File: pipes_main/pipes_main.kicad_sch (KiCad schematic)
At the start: 51 parts, among them J1 3.5mm Jack, J10 3.5mm Jack, J11 3.5mm Jack, J12 3.5mm Jack, J21 2x8 Female Header, J22 2x5 Female Header, J4 3.5mm Jack, J5 3.5mm Jack, J6 3.5mm Jack, J7 3.5mm Jack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

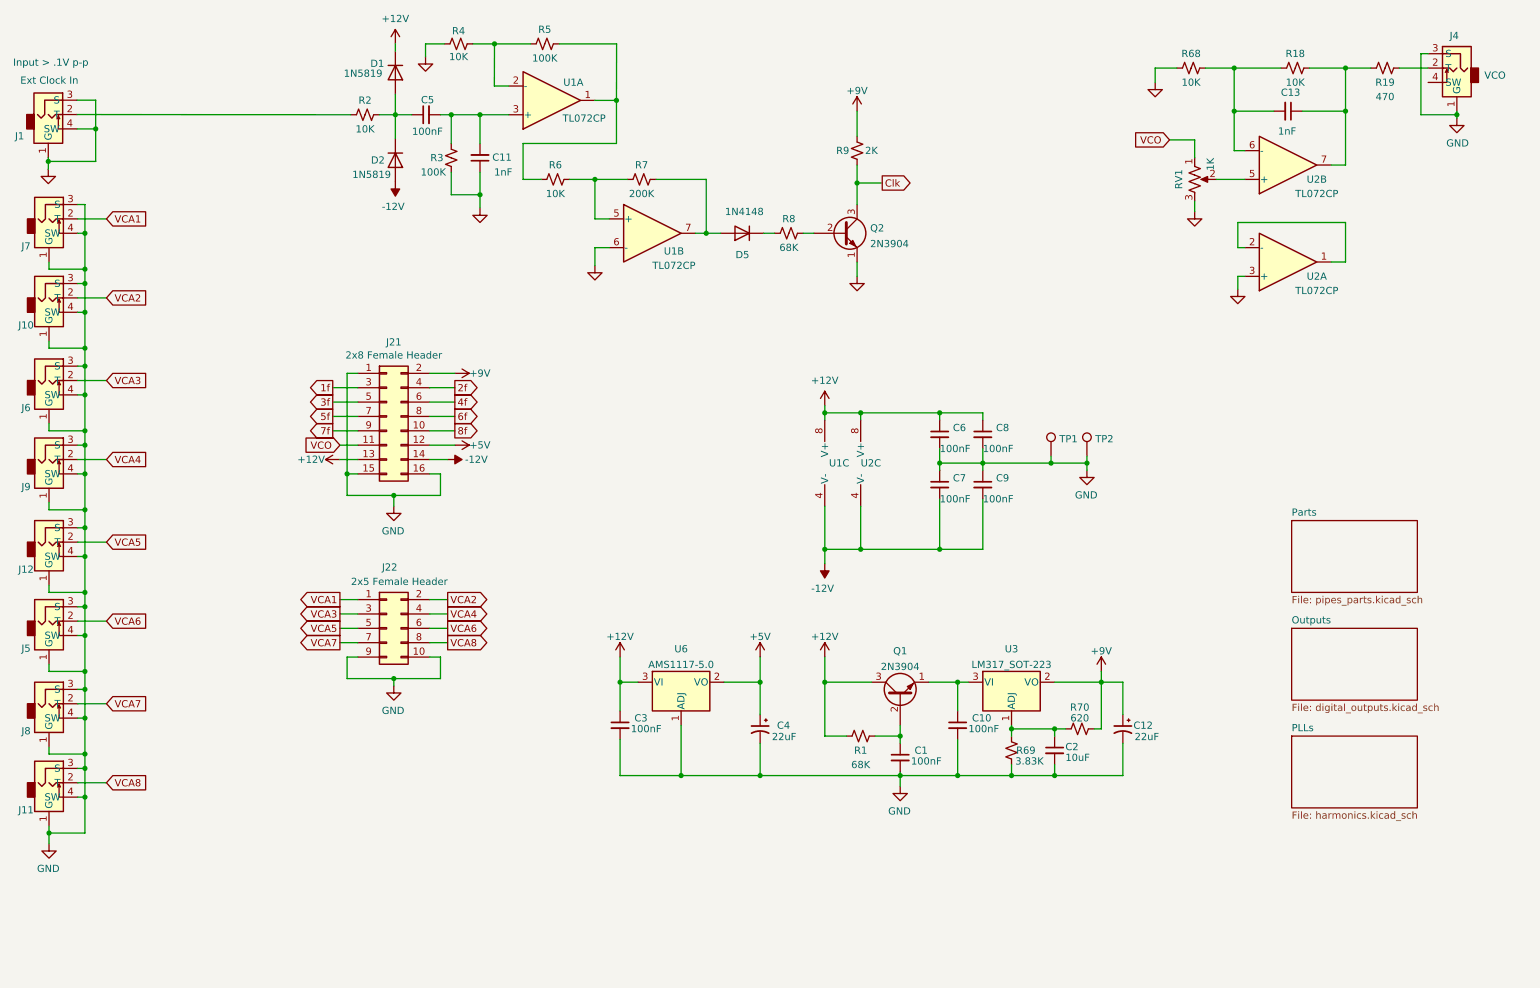
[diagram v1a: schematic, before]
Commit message: Updates component values. Uses .5W resistors on outputs now.
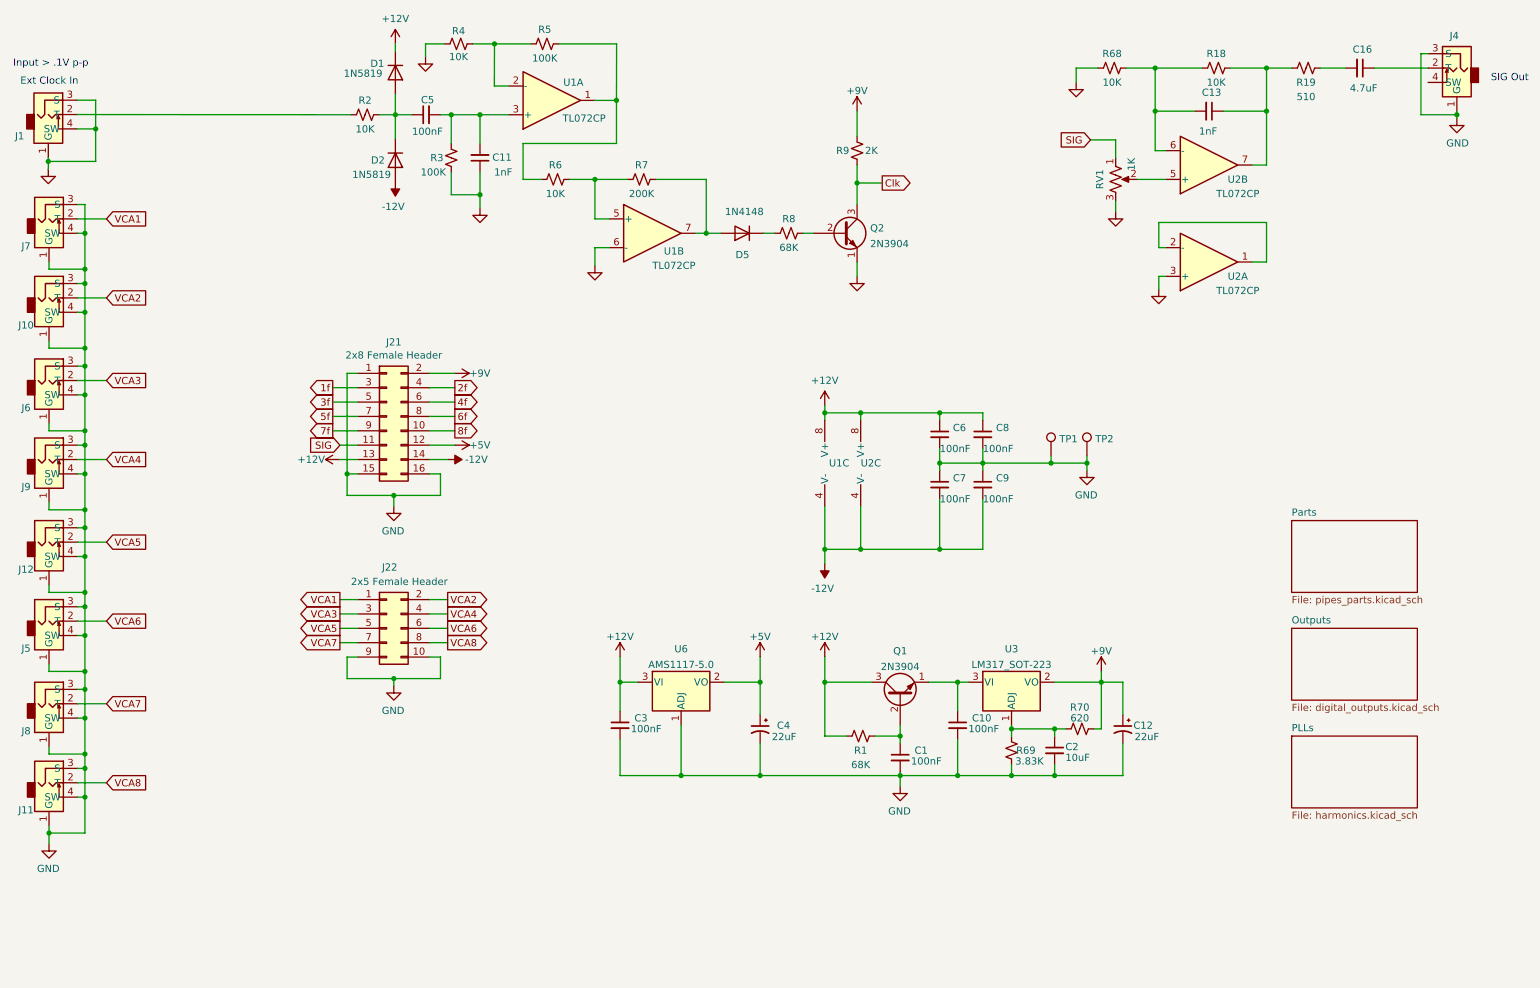
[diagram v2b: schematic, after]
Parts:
- added C16: 4.7uF, Capacitor_SMD:C_1206_3216Metric, symbol Device:C_Small
- R19: value 470 -> 510; LCSC Part # C17710 -> C2842425
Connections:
- net at R19.2: now also C16.2; no longer J4.2 (T)
- net VCO renamed SIG
- new net: C16.1, J4.2 (T)
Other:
- note added: "SIG Out"
- note removed: "VCO"
- moved on the sheet: C13, R18, R19, R68, RV1, U2A, U2B

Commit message: Adds digikey bom merge. Uses local graphics for panel.
Adds bambooh graphics
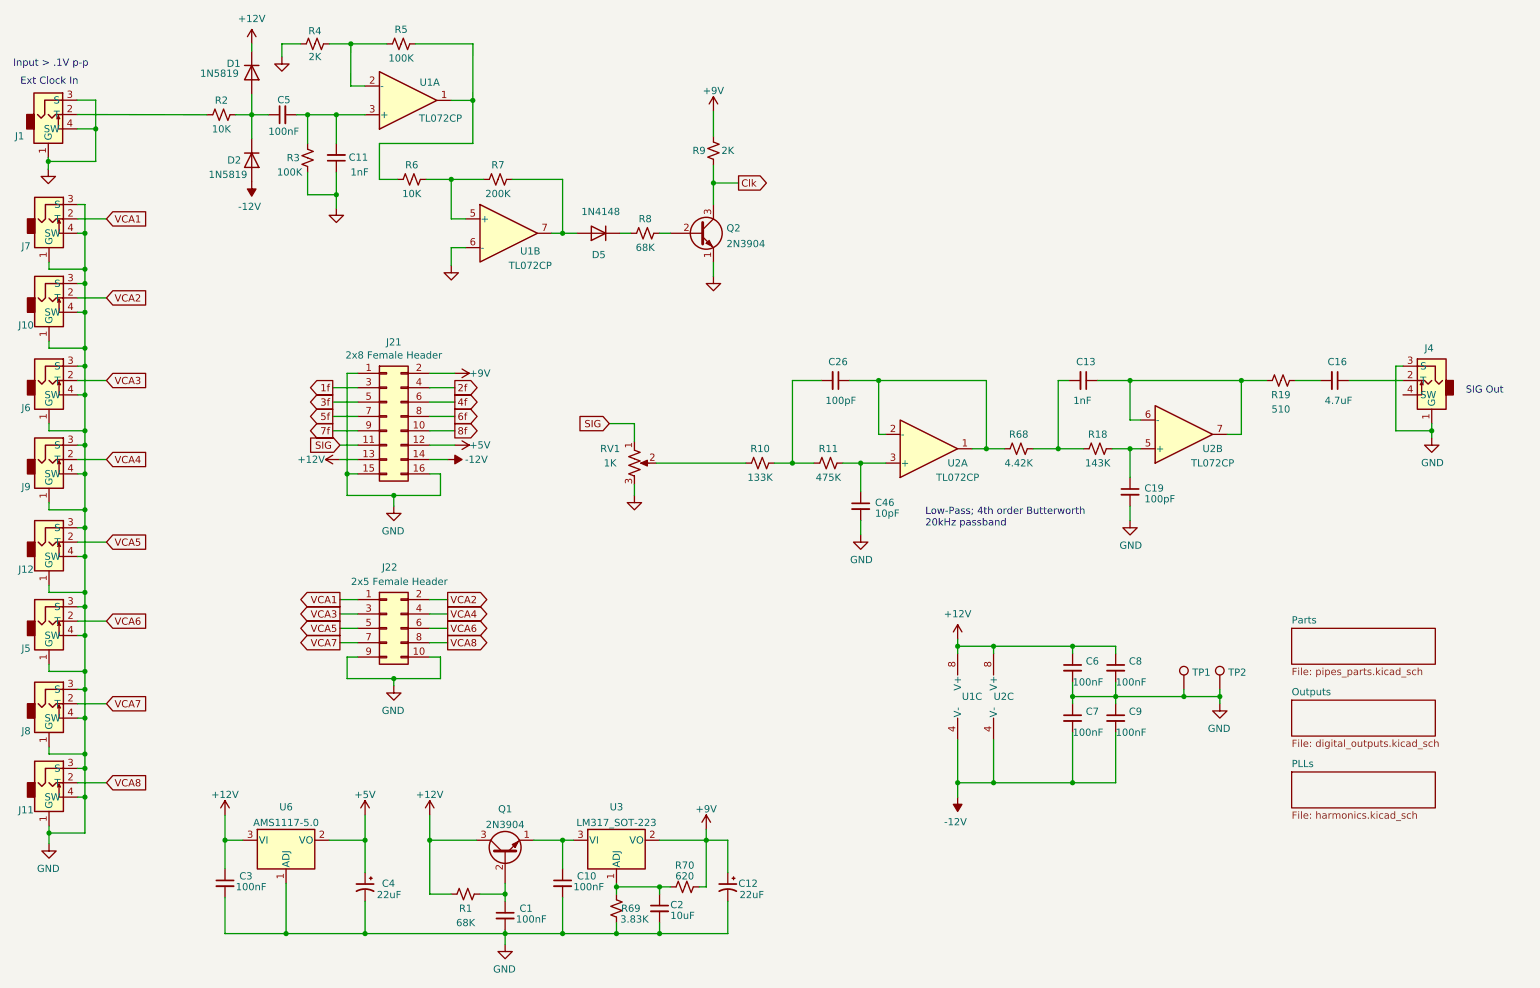
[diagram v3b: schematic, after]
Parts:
- added C19, C26: 100pF, Capacitor_SMD:C_0805_2012Metric_Pad1.18x1.45mm_HandSolder, symbol Device:C_Small
- added C46: 10pF, Capacitor_SMD:C_0805_2012Metric_Pad1.18x1.45mm_HandSolder, symbol Device:C_Small
- added R10: 133K, Resistor_SMD:R_0603_1608Metric, symbol Device:R_Small_US
- added R11: 475K, Resistor_SMD:R_0603_1608Metric, symbol Device:R_Small_US
- C13: LCSC Part # C46653 -> C597357
- R18: value 10K -> 143K; LCSC Part # C25804 -> C304703
- R4: value 10K -> 2K; LCSC Part # C25804 -> C22975
- R68: value 10K -> 4.42K; LCSC Part # C25804 -> C23043
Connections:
- net GND: now also C19.2, C46.2; no longer R68.2, U2.3 (+)
- net at C13.1, R19.1, U2.7: now also U2.6 (-); no longer R18.1
- net at C13.2, R18.2, R68.1: no longer U2.6 (-)
- net at U2.5 (+): now also R18.1, C19.1; no longer RV1.2
- net at U2.1, U2.2 (-): now also R68.2, C26.1
- new net: C26.2, R10.1, R11.2
- new net: R10.2, RV1.2
- new net: C46.1, R11.1, U2.3 (+)
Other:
- note added: "Low-Pass; 4th order Butterworth 20kHz passband"
- moved on the sheet: C1, C10, C11, C12, C13, C16, C2, C3, C4, C5, C6, C7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
